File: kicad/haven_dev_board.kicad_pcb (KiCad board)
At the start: 6 copper layers, 72.9 x 160.9 mm, 89 parts, among them CN1 BM46B-12DS-0.35V(51).1, J1 CLE-107-01-G-DV.1, Q1 CSD23382F4.1, Q2 CSD13380F3T.1, Q3 CSD13380F3T.1, SW1 TS2819A 230GF.1, U1 BMX160.1, U10 SN74AXC4T774RSVR.1, U12 GT-USB-9047A.1, U13 SPH0641LU4H-1.1, U14 MX25R6435FBFIL0.1, U15 ADAU1860BCBZRL.1, U2 BQ25120AYFPR.1, U3 AP22916BCA4-7.1, U4 XL-0201SURC.1, U5 KTD2026.1, U6 BQ27220YZFR.1, U8 1MΩ.1, U9 AP22916BCA4-7.1, X1 Q13FC1350000200.1

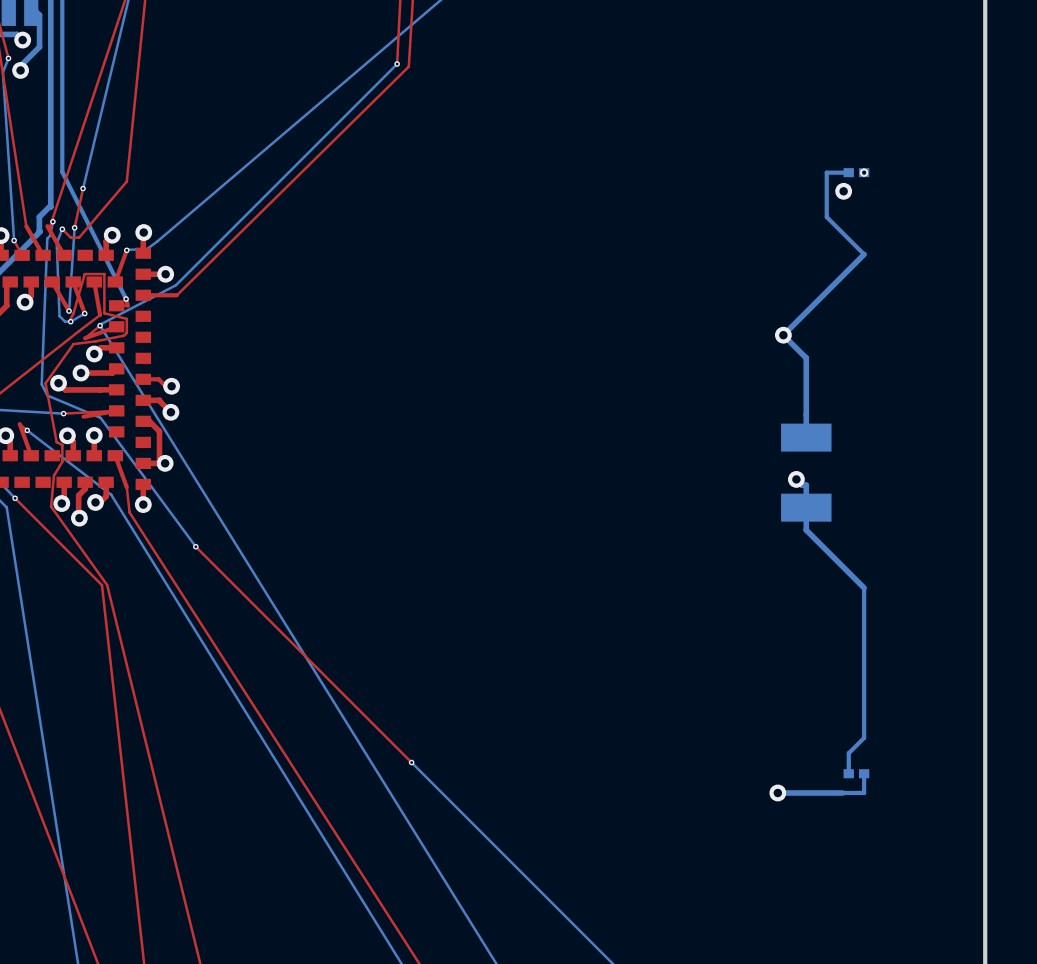
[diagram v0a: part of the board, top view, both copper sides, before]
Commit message: Move X1 (32.768 kHz) + C2/C14 behind MDBT531 XL1/XL2; DRC 219 -> 219, 0 new
The 5x rescale left the nRF5340's LFXO crystal 30.4 mm from the module
(load caps 10.9 mm away). X1 now sits on B.Cu directly behind pins 34/36,
fed from the two existing module-edge through-vias (kept, with their F.Cu
pin stubs); C14/C2 sit against the crystal pads with their own GND vias
to the In1/In2 planes. XL1/XL2 copper: 36 mm each -> ~2.3 mm each.
Stale XL1/XL2 In1 long-hauls, far vias and the orphaned GND stubs at the
old cap positions removed.

kicad-cli 9.0.8 DRC (routing-evidence/placement-fix/): 219 -> 219
violations, 2 -> 2 unconnected, zero new (type, description) identities.
Tools: placement_lib.py (pcbnew spot finder / move / route checks),
drc_diff.py (identity diff), remove_items_by_uuid.py + clean_dangling.sh
(text-level cleanup of orphaned stubs the DRC report names by uuid).

Co-Authored-By: Claude Fable 5.1 <noreply@anthropic.com>
Claude-Session: https://claude.ai/code/session_01K7G9Bv5agmyedmt776NSLV
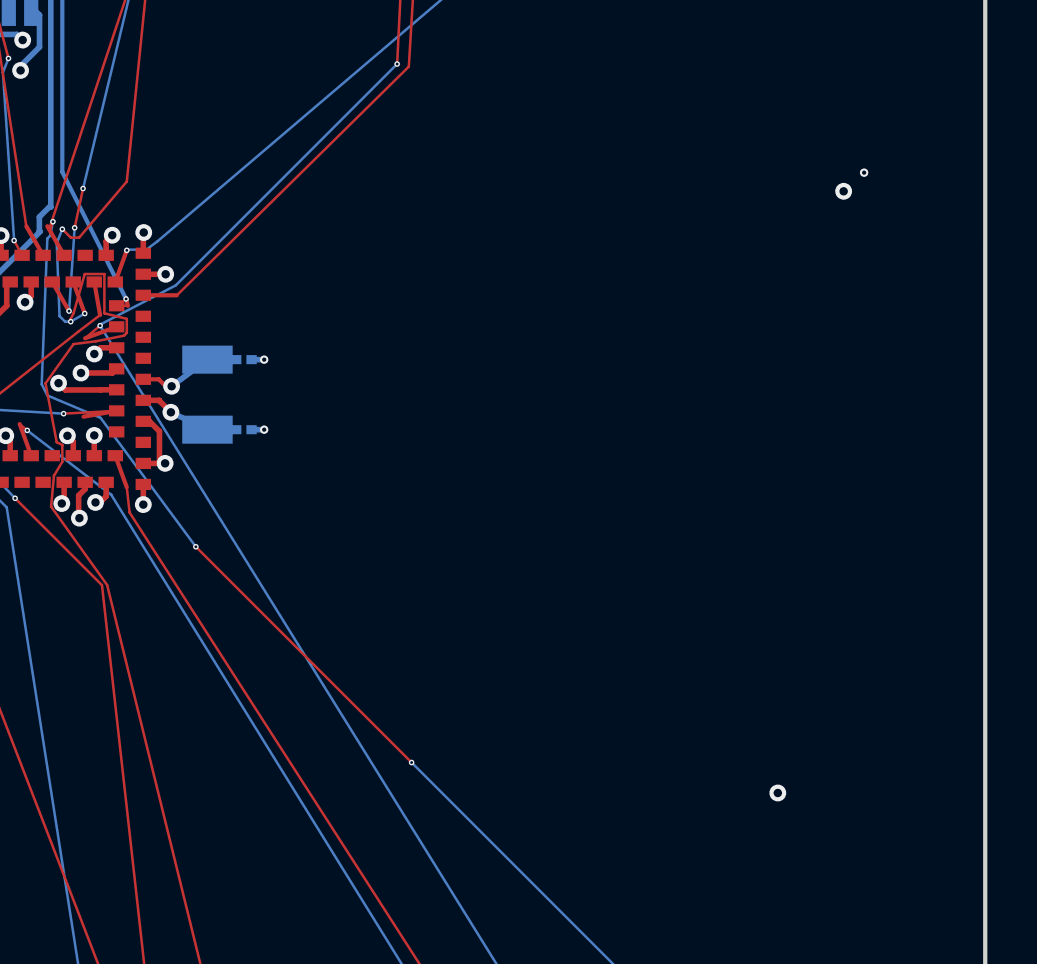
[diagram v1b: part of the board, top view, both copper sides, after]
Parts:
- moved C2 25.1 mm to (88.4, 72.1)
- moved C14 22.9 mm to (88.4, 69.7)
- moved X1 21.6 mm to (87.1, 70.9)
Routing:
- net XL2: track 36.3 -> 3.64 mm, vias 2 -> 1
- net XL1: track 36.0 -> 3.73 mm, vias 2 -> 1
- net GND: track 665.2 -> 662.3 mm, vias 56 -> 58
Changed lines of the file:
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@@
 	(footprint "haven_footprints:C0201"
 		(layer "B.Cu")
-		(at 110.2598 62.9777)
+		(at 88.4 69.65)
 		(property "Reference" "C14"
 			(at 0 -1.5 0)
@@
 	(footprint "haven_footprints:FC-135R_L3.2-W1.5"
 		(layer "B.Cu")
-		(at 108.4698 73.6827)
+		(at 87.1 70.9)
 		(property "Reference" "X1"
 			(at 0 -1.5 0)
@@
 	(footprint "haven_footprints:C0201"
 		(layer "B.Cu")
-		(at 110.2598 84.4277)
+		(at 88.4 72.1499)
 		(property "Reference" "C2"
 			(at 0 -1.5 0)
@@
 	)
 	(via
+		(at 89.1243 72.1498)
+		(size 0.3)
+		(drill 0.15)
+		(layers "F.Cu" "B.Cu")
+		(net 25)
+	)
+	(via
 		(at 109.0097 1.552)
 		(size 0.3)
@@
 	)
 	(via
+		(at 89.1243 69.6499)
+		(size 0.3)
+		(drill 0.15)
+		(layers "F.Cu" "B.Cu")
+		(net 25)
+	)
+	(via
 		(at 76.2 74.5277)
 		(size 0.3)
@@
 	)
 	(segment
-		(start 110.5341 84.4276)
-		(end 110.5341 85.1149)
-		(width 0.15)
-		(locked yes)
-		(layer "B.Cu")
-		(net 25)
-	)
-	(segment
 		(start 68.7 131.8534)
 		(end 69.4102 131.8534)
@@
 	)
 	(segment
+		(start 88.6743 69.6499)
+		(end 89.1243 69.6499)
+		(width 0.2)
+		(layer "B.Cu")
+		(net 25)
+	)
+	(segment
 		(start 79.1404 32.0837)
 		(end 78.4687 32.0837)
@@
 	)
 	(segment
-		(start 109.762 85.1149)
-		(end 107.4546 85.1149)
+		(start 76.8712 26.5514)
+		(end 77.3 26.5514)
 		(width 0.2)
 		(locked yes)
@@
 	)
 	(segment
-		(start 76.8712 26.5514)
-		(end 77.3 26.5514)
+		(start 88.6743 72.1498)
+		(end 89.1243 72.1498)
 		(width 0.2)
-		(locked yes)
 		(layer "B.Cu")
 		(net 25)
@@
 	)
 	(segment
-		(start 110.5341 85.1149)
-		(end 109.762 85.1149)
-		(width 0.15)
-		(locked yes)
-		(layer "B.Cu")
-		(net 25)
-	)
-	(segment
 		(start 94.4919 34.7277)
 		(end 95 34.7277)
@@
 	)
 	(via
-		(at 107.6522 68.7773)
-		(size 0.6)
-		(drill 0.3)
-		(layers "F.Cu" "B.Cu")
-		(locked yes)
-		(net 81)
-	)
-	(via
 		(at 85.8201 70.6009)
 		(size 0.6)
@@
 	)
 	(segment
-		(start 109.2 62.9776)
-		(end 109.2 64.5617)
-		(width 0.15)
-		(locked yes)
-		(layer "B.Cu")
-		(net 81)
-	)
-	(segment
-		(start 109.9855 62.9776)
-		(end 109.2 62.9776)
-		(width 0.15)
-		(locked yes)
-		(layer "B.Cu")
-		(net 81)
-	)
-	(segment
-		(start 108.4699 72.4327)
-		(end 108.47 72.4327)
-		(width 0.2)
-		(layer "B.Cu")
-		(net 81)
-	)
-	(segment
-		(start 108.4699 72.4327)
-		(end 108.4699 71.631)
-		(width 0.2)
-		(locked yes)
-		(layer "B.Cu")
-		(net 81)
-	)
-	(segment
-		(start 108.4699 69.595)
-		(end 108.4699 71.631)
-		(width 0.2)
-		(locked yes)
-		(layer "B.Cu")
-		(net 81)
-	)
-	(segment
-		(start 109.2 64.5617)
-		(end 110.5339 65.8956)
-		(width 0.15)
-		(locked yes)
-		(layer "B.Cu")
-		(net 81)
-	)
-	(segment
-		(start 107.6522 68.7773)
-		(end 108.4699 69.595)
+		(start 85.82 70.601)
+		(end 87.1001 69.65)
 		(width 0.2)
-		(locked yes)
 		(layer "B.Cu")
 		(net 81)
 	)
 	(segment
-		(start 107.6522 68.7773)
-		(end 110.5339 65.8956)
+		(start 87.1001 69.65)
+		(end 88.1257 69.6499)
 		(width 0.2)
-		(locked yes)
 		(layer "B.Cu")
 		(net 81)
 	)
 	(segment
-		(start 87.6437 68.7773)
-		(end 107.6522 68.7773)
-		(width 0.2)
-		(locked yes)
-		(layer "In1.Cu")
-		(net 81)
-	)
-	(segment
-		(start 85.8201 70.6009)
-		(end 87.6437 68.7773)
-		(width 0.2)
-		(locked yes)
-		(layer "In1.Cu")
-		(net 81)
-	)
-	(segment
 		(start 84.8102 71.1027)
 		(end 85.3869 71.1027)
@@
 	)
 	(via
-		(at 108.1176 73.924)
-		(size 0.6)
-		(drill 0.3)
-		(layers "F.Cu" "B.Cu")
-		(locked yes)
-		(net 82)
-	)
-	(via
 		(at 85.7955 71.5291)
 		(size 0.6)
@@
 	)
 	(segment
-		(start 108.4699 75.7343)
-		(end 110.5339 77.7983)
+		(start 87.1001 72.1499)
+		(end 88.1257 72.1498)
 		(width 0.2)
-		(locked yes)
 		(layer "B.Cu")
 		(net 82)
 	)
 	(segment
-		(start 108.3245 74.1309)
-		(end 108.1176 73.924)
+		(start 85.796 71.529)
+		(end 87.1001 72.1499)
 		(width 0.2)
-		(locked yes)
-		(layer "B.Cu")
-		(net 82)
-	)
-	(segment
-		(start 109.9855 83.6984)
-		(end 110.5339 83.15)
-		(width 0.15)
-		(locked yes)
 		(layer "B.Cu")
 		(net 82)
 	)
-	(segment
-		(start 108.4699 74.9326)
-		(end 108.47 74.9326)
-		(width 0.2)
-		(layer "B.Cu")
-		(net 82)
-	)
-	(segment
-		(start 108.4699 74.9326)
-		(end 108.4699 75.7343)
-		(width 0.2)
-		(locked yes)
-		(layer "B.Cu")
-		(net 82)
-	)
-	(segment
-		(start 110.5339 83.15)
-		(end 110.5339 77.7983)
-		(width 0.15)
-		(locked yes)
-		(layer "B.Cu")
-		(net 82)
-	)
-	(segment
-		(start 108.4699 74.1309)
-		(end 108.3245 74.1309)
-		(width 0.2)
-		(locked yes)
-		(layer "B.Cu")
-		(net 82)
-	)
-	(segment
-		(start 109.9855 84.4276)
-		(end 109.9855 83.6984)
-		(width 0.15)
-		(locked yes)
-		(layer "B.Cu")
-		(net 82)
-	)
-	(segment
-		(start 108.4699 74.9326)
-		(end 108.4699 74.1309)
-		(width 0.2)
-		(locked yes)
-		(layer "B.Cu")
-		(net 82)
-	)
-	(segment
-		(start 88.1904 73.924)
-		(end 85.7955 71.5291)
-		(width 0.2)
-		(locked yes)
-		(layer "In1.Cu")
-		(net 82)
-	)
-	(segment
-		(start 108.1176 73.924)
-		(end 88.1904 73.924)
-		(width 0.2)
-		(locked yes)
-		(layer "In1.Cu")
-		(net 82)
-	)

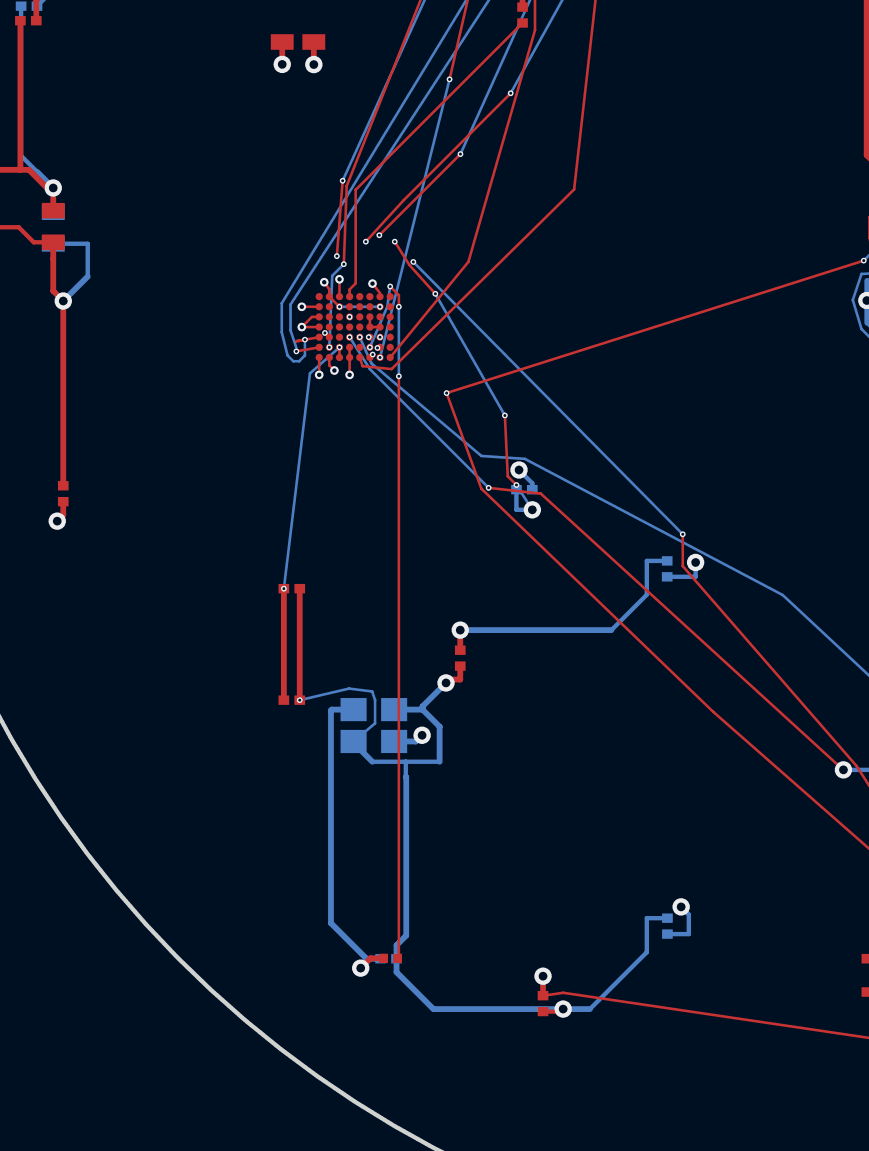
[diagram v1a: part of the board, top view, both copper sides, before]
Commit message: Move CRYSTAL1 (24.576 MHz) + C45/C46 + R28 next to U15 XTALI/XTALO; DRC 219 -> 219, 0 new
Crystal centre 13.8 mm -> 5.2 mm from the ADAU1860 (load caps were 8.1/9.7 mm
from the crystal, now 1.7/2.1 mm; R28 21.8 -> 3.9 mm), all four parts on
B.Cu just NE of the BGA.

Why the first attempt failed: the two kept escape vias sit in a B.Cu pocket
walled off by TDO/SDA1/DOUT diagonals, and the XTALO escape hugs TDO at
0.11 mm -- legal only through the .kicad_dru per-pair exceptions
(XTALO/TDO 0.05, /V_LS 0.05, /SDA1 0.05, /XTALI 0.03; XTALI/TDO 0.015). The
plain 0.20 mm A* saw the via start as blocked. This routes XTALI/XTALO with
multilayer_astar_mixed under exactly those exceptions (F.Cu hop over TDO,
one new via each, pad end forced onto B.Cu), everything else single-layer
B.Cu; GND pads get 0.20/0.10 vias into the planes. R28's placement search no
longer ignores the crystal (that produced a GND/XTALO short in an earlier
pass). Stale GND stubs at the old positions removed; the XTALO escape via
whose F.Cu side became unused removed (via_dangling).

kicad-cli 9.0.8 drc --severity-all --all-track-errors:
  after group A : 219 violations / 2 unconnected
  after group B : 219 violations / 2 unconnected, 0 new (type+description)
tools/remove_items_by_uuid.py: accept uuid prefixes. tools/measure_placement.py: the §0.7 distance table.

Co-Authored-By: Claude Fable 5.1 <noreply@anthropic.com>
Claude-Session: https://claude.ai/code/session_01K7G9Bv5agmyedmt776NSLV
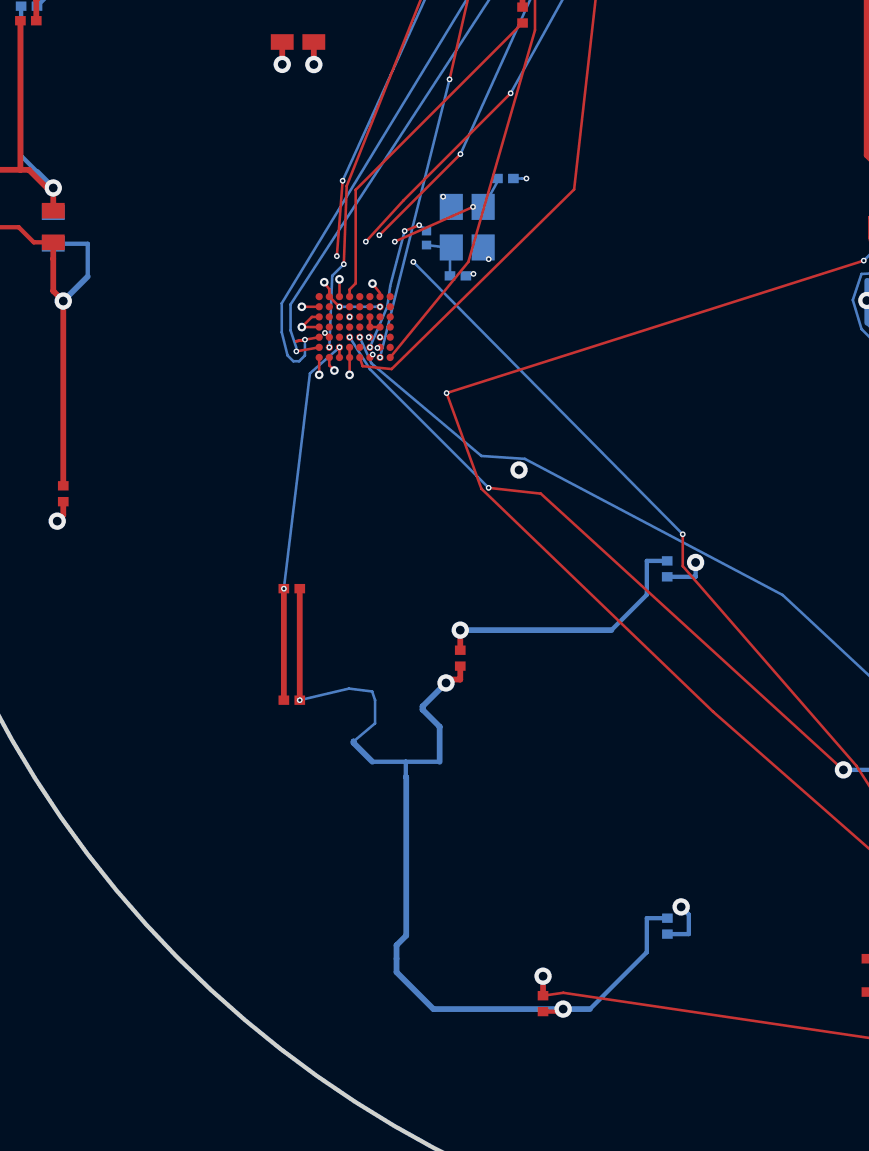
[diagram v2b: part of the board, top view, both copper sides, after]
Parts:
- R28: moved to B.Cu
- moved R28 24.9 mm to (61.1, 108.4), turned to 90 degrees
- moved C45 23.7 mm to (62.2, 109.7)
- moved CRYSTAL1 17.5 mm to (62.5, 108.0), turned to 90 degrees
- moved C46 10.8 mm to (63.8, 106.3)
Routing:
- net XTALO: track 25.6 -> 5.09 mm, vias 4 -> 3
- net XTALI: track 26.9 -> 9.02 mm, vias 7 -> 3
- net $1N16368: track 11.7 -> 1.89 mm, vias 1 -> 0
- net GND: vias 58 -> 62

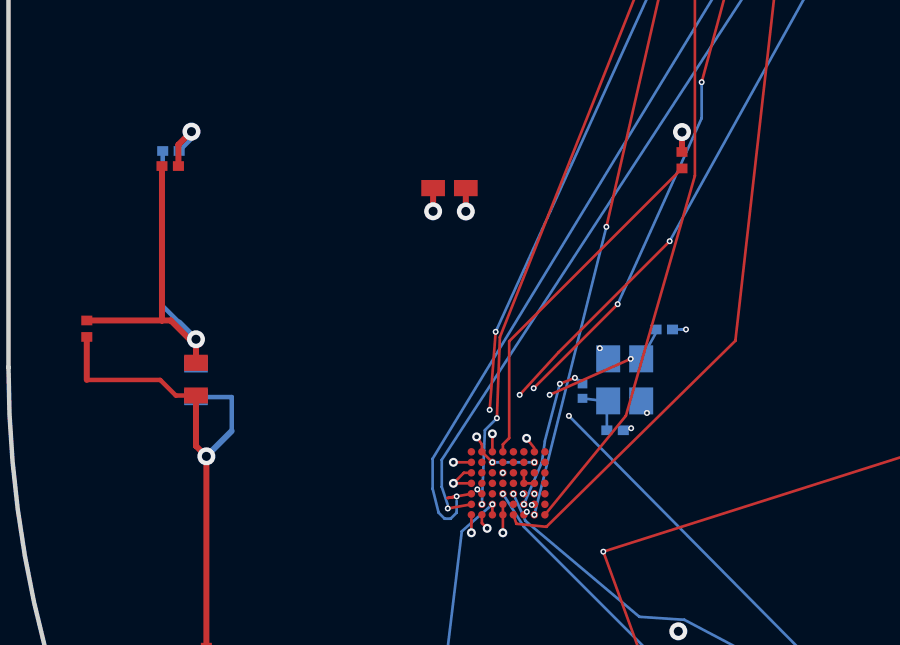
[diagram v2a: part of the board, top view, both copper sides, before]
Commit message: Move C33 (V_LS 10 uF) to 2.0 mm from U15's supply balls; DRC 219 -> 219, 0 new
Was 10.0 mm away at (56.66,101.61); now (56.69,109.90) on F.Cu, V_LS pad
routed to the existing V_LS via at the BGA's F3/F7 escape, GND pad on its
own 0.20/0.10 via. The old V_LS run north to the previous position (F.Cu
segments + via + an In3.Cu piece) removed as it became dangling.

New tool tools/move_two_terminal.py (generic two-terminal relocation with
DRC-clean routing). One defect fixed while writing it: a track END on an
inner layer must never be a routing anchor -- the first pass routed the pad
on F.Cu to the end of an In3.Cu track, which connects nothing; anchors are
now IC pads, through-vias, and outer-layer track ends with a matching start
layer.

kicad-cli 9.0.8: 219 violations / 2 unconnected before and after.

Co-Authored-By: Claude Fable 5.1 <noreply@anthropic.com>
Claude-Session: https://claude.ai/code/session_01K7G9Bv5agmyedmt776NSLV
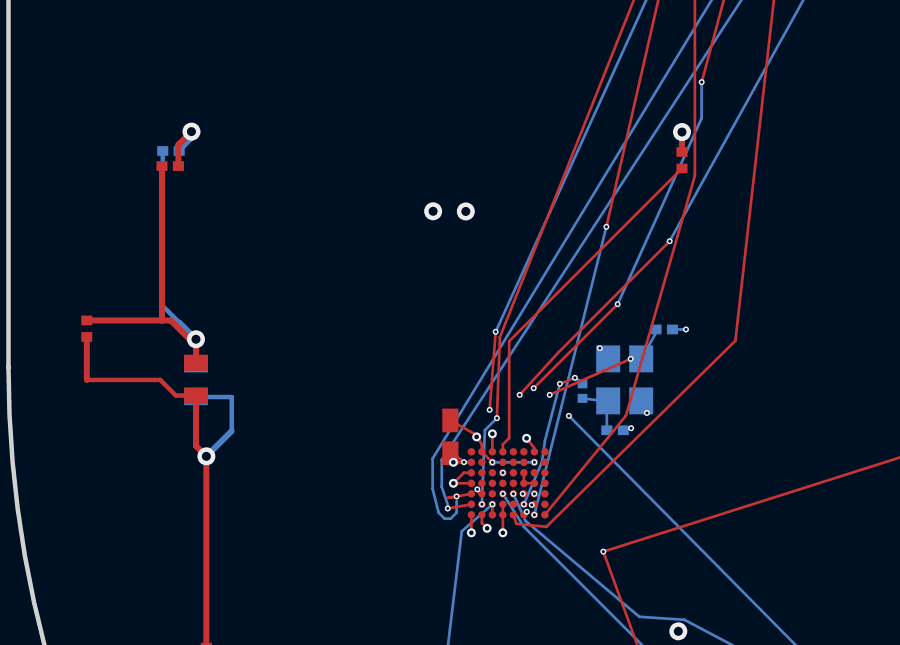
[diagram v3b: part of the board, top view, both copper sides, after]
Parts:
- moved C33 8.29 mm to (56.7, 109.9), turned to 90 degrees
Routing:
- net GND: track 662.3 -> 662.1 mm, vias 62 -> 63
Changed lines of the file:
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@@
 	(footprint "haven_footprints:C0402"
 		(layer "F.Cu")
-		(at 56.6598 101.6077)
+		(at 56.69 109.898 90)
 		(property "Reference" "C33"
-			(at 0 -1.5 0)
+			(at 0 -1.5 90)
 			(layer "F.SilkS")
 			(hide yes)
@@
 		)
 		(property "Value" "10uF.1"
-			(at 0 1.5 0)
+			(at 0 1.5 90)
 			(layer "F.Fab")
 			(hide yes)
@@
 		)
 		(property "Datasheet" ""
-			(at 0 0 0)
+			(at 0 0 90)
 			(layer "F.Fab")
 			(hide yes)
@@
 		)
 		(property "Description" ""
-			(at 0 0 0)
+			(at 0 0 90)
 			(layer "F.Fab")
 			(hide yes)
@@
 		(attr smd)
 		(pad "1" smd rect
-			(at -0.5451 0.0001)
+			(at -0.5451 0.0001 90)
 			(size 0.7901 0.54)
 			(layers "F.Cu" "F.Mask" "F.Paste")
@@
 		)
 		(pad "2" smd rect
-			(at 0.545 0.0001)
+			(at 0.545 0.0001 90)
 			(size 0.7901 0.54)
 			(layers "F.Cu" "F.Mask" "F.Paste")
@@
 	)
 	(segment
-		(start 56.1147 101.608)
-		(end 56.1147 101.6078)
-		(width 0.2)
-		(layer "F.Cu")
-		(net 25)
-	)
-	(segment
 		(start 47.0765 100.873)
 		(end 47.0765 100.8727)
@@
 	)
 	(segment
-		(start 56.1147 102.3807)
-		(end 56.1147 101.6078)
-		(width 0.2)
-		(locked yes)
+		(start 56.6901 110.4431)
+		(end 57.1901 110.7431)
+		(width 0.09)
 		(layer "F.Cu")
 		(net 25)
@@
 	)
 	(via
+		(at 57.144278 110.744604)
+		(size 0.2)
+		(drill 0.1)
+		(layers "F.Cu" "B.Cu")
+		(net 25)
+	)
+	(via
 		(at 108.5833 29.1035)
 		(size 0.6)
@@
 	)
 	(segment
-		(start 44.5703 108.0024)
-		(end 47.0188 108.0024)
-		(width 0.15)
-		(locked yes)
+		(start 57.5901 109.853)
+		(end 56.6901 109.353)
+		(width 0.09)
 		(layer "F.Cu")
 		(net 78)
 	)
 	(segment
-		(start 57.2048 101.608)
-		(end 57.2048 101.6078)
-		(width 0.2)
+		(start 44.5703 108.0024)
+		(end 47.0188 108.0024)
+		(width 0.15)
+		(locked yes)
 		(layer "F.Cu")
 		(net 78)
@@
 		(layer "F.Cu")
 		(net 78)
-	)
-	(segment
-		(start 57.2048 102.3864)
-		(end 57.2048 101.6078)
-		(width 0.2)
-		(locked yes)
-		(layer "F.Cu")
-		(net 78)
